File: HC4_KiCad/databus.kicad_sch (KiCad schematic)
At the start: 11 parts, among them IC10 74HC4002, IC8 74HC257, IC9 74HC244, J3 Expantion_Connector

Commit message: 回路の改良　試験は明日やる
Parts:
- added RN2: 10k, Resistor_THT:R_Array_SIP9, symbol Device:R_Network08_Split
- renumbered RN2 to RN1
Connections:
- net Databus0: now also RN2.2 (R1.2)
- net Databus1: now also RN2.3 (R2.2)
- net Databus2: now also RN2.4 (R3.2)
- net Databus3: now also RN2.5 (R4.2)
- net VCC: now also RN2.1 (R1), RN2.1 (R1), RN2.1 (R1), RN2.1 (R1), RN2.1 (R1), RN2.1 (R1), RN2.1 (R1), RN2.1 (R1)
- net Dummy7: now reaches J3.10 (Pin_10)
- net Dummy7: now also RN2.9 (R8.2)
- net Dummy4: now reaches J3.7 (Pin_7)
- net Dummy4: now also RN2.6 (R5.2)
- net Dummy5: now reaches J3.8 (Pin_8)
- net Dummy5: now also RN2.7 (R6.2)
- net Dummy6: now reaches J3.9 (Pin_9)
- net Dummy6: now also RN2.8 (R7.2)
- no-connect marks 22 -> 18

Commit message: フットプリントをSOPに変更
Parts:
- CP8, CP9: footprint Capacitor_THT:C_Disc_D3.0mm_W1.6mm_P2.50mm -> Capacitor_SMD:C_0603_1608Metric
- IC10: footprint Package_DIP:DIP-14_W7.62mm_Socket -> Package_SO:SO-14_5.3x10.2mm_P1.27mm
- IC8: footprint Package_DIP:DIP-16_W7.62mm_Socket -> Package_SO:SO-16_5.3x10.2mm_P1.27mm
- IC9: footprint Package_DIP:DIP-20_W7.62mm_Socket -> Package_SO:SOP-20_7.5x12.8mm_P1.27mm
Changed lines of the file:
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@@
 			)
 		)
-		(property "Footprint" "Capacitor_THT:C_Disc_D3.0mm_W1.6mm_P2.50mm"
+		(property "Footprint" "Capacitor_SMD:C_0603_1608Metric"
 			(at 147.0152 163.83 0)
 			(effects
@@
 			)
 		)
-		(property "Footprint" "Package_DIP:DIP-20_W7.62mm_Socket"
+		(property "Footprint" "Package_SO:SOP-20_7.5x12.8mm_P1.27mm"
 			(at 99.06 133.35 0)
 			(effects
@@
 			)
 		)
-		(property "Footprint" "Package_DIP:DIP-16_W7.62mm_Socket"
+		(property "Footprint" "Package_SO:SO-16_5.3x10.2mm_P1.27mm"
 			(at 99.06 72.39 0)
 			(effects
@@
 			)
 		)
-		(property "Footprint" "Capacitor_THT:C_Disc_D3.0mm_W1.6mm_P2.50mm"
+		(property "Footprint" "Capacitor_SMD:C_0603_1608Metric"
 			(at 153.3652 163.83 0)
 			(effects
@@
 			)
 		)
-		(property "Footprint" "Package_DIP:DIP-14_W7.62mm_Socket"
+		(property "Footprint" "Package_SO:SO-14_5.3x10.2mm_P1.27mm"
 			(at 144.78 64.77 0)
 			(effects

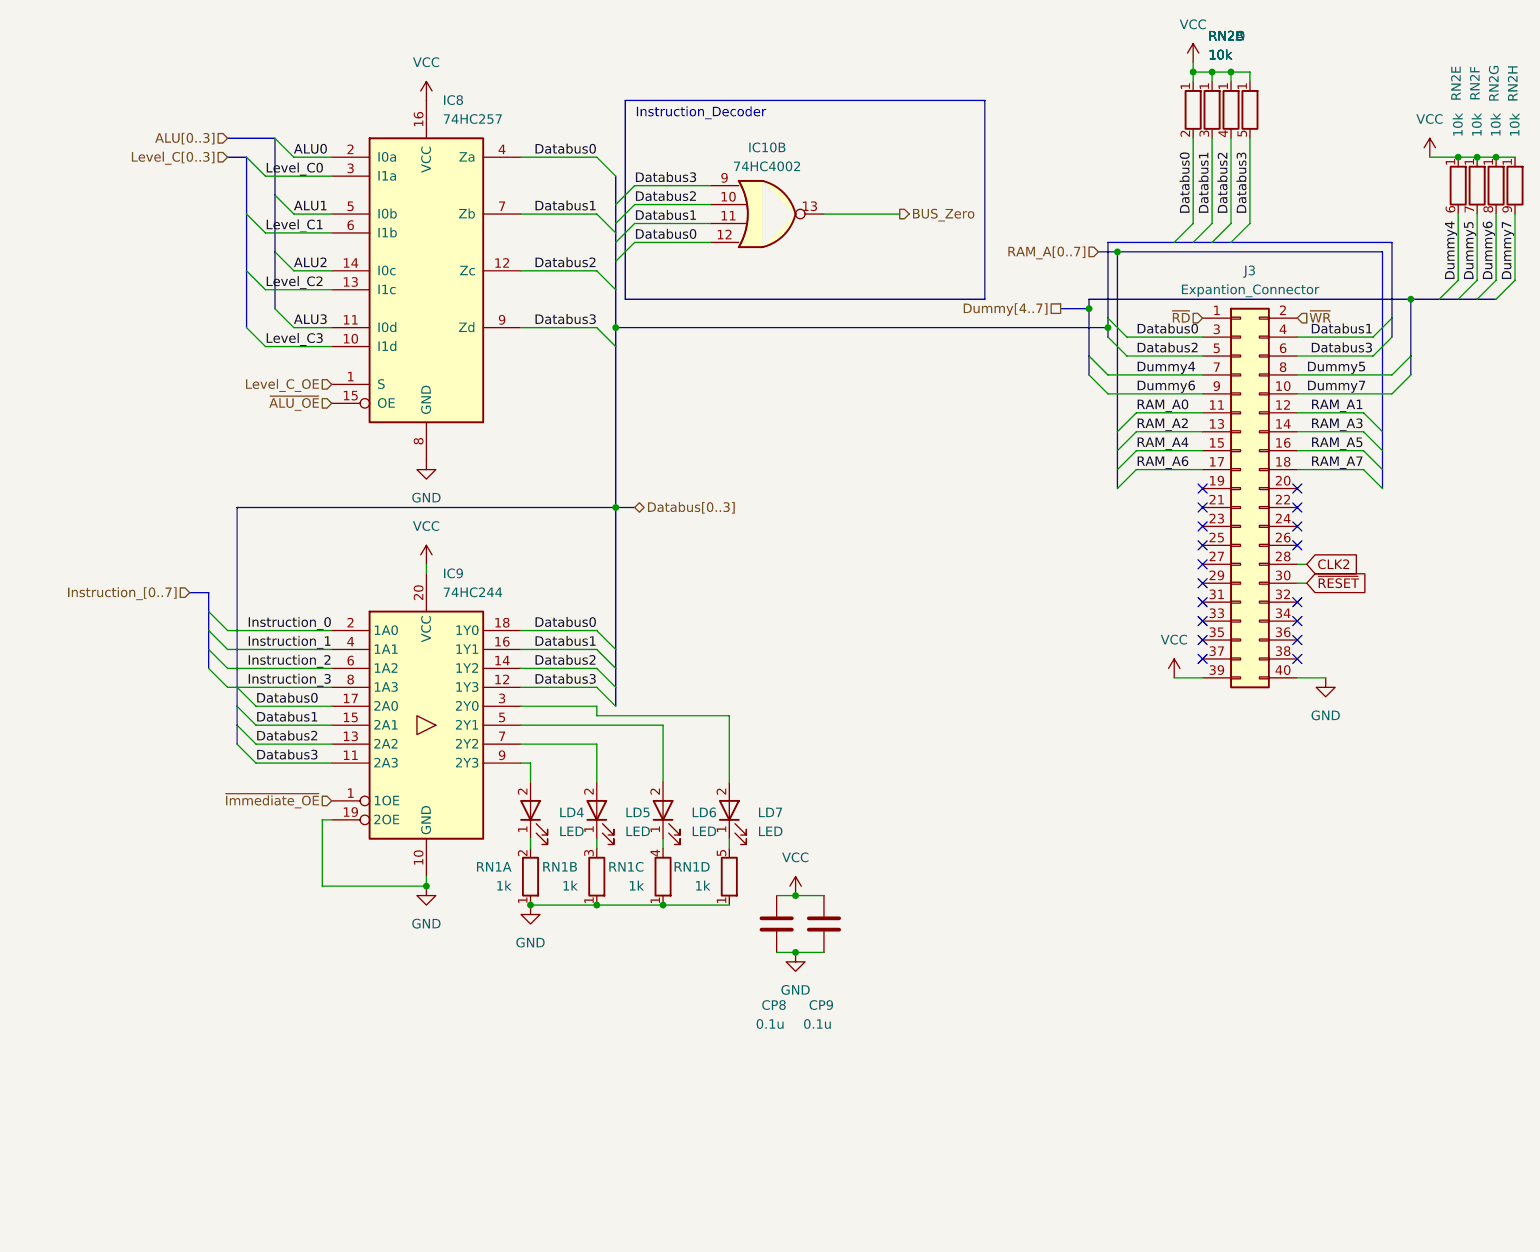
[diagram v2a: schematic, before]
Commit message: Added output port for blink
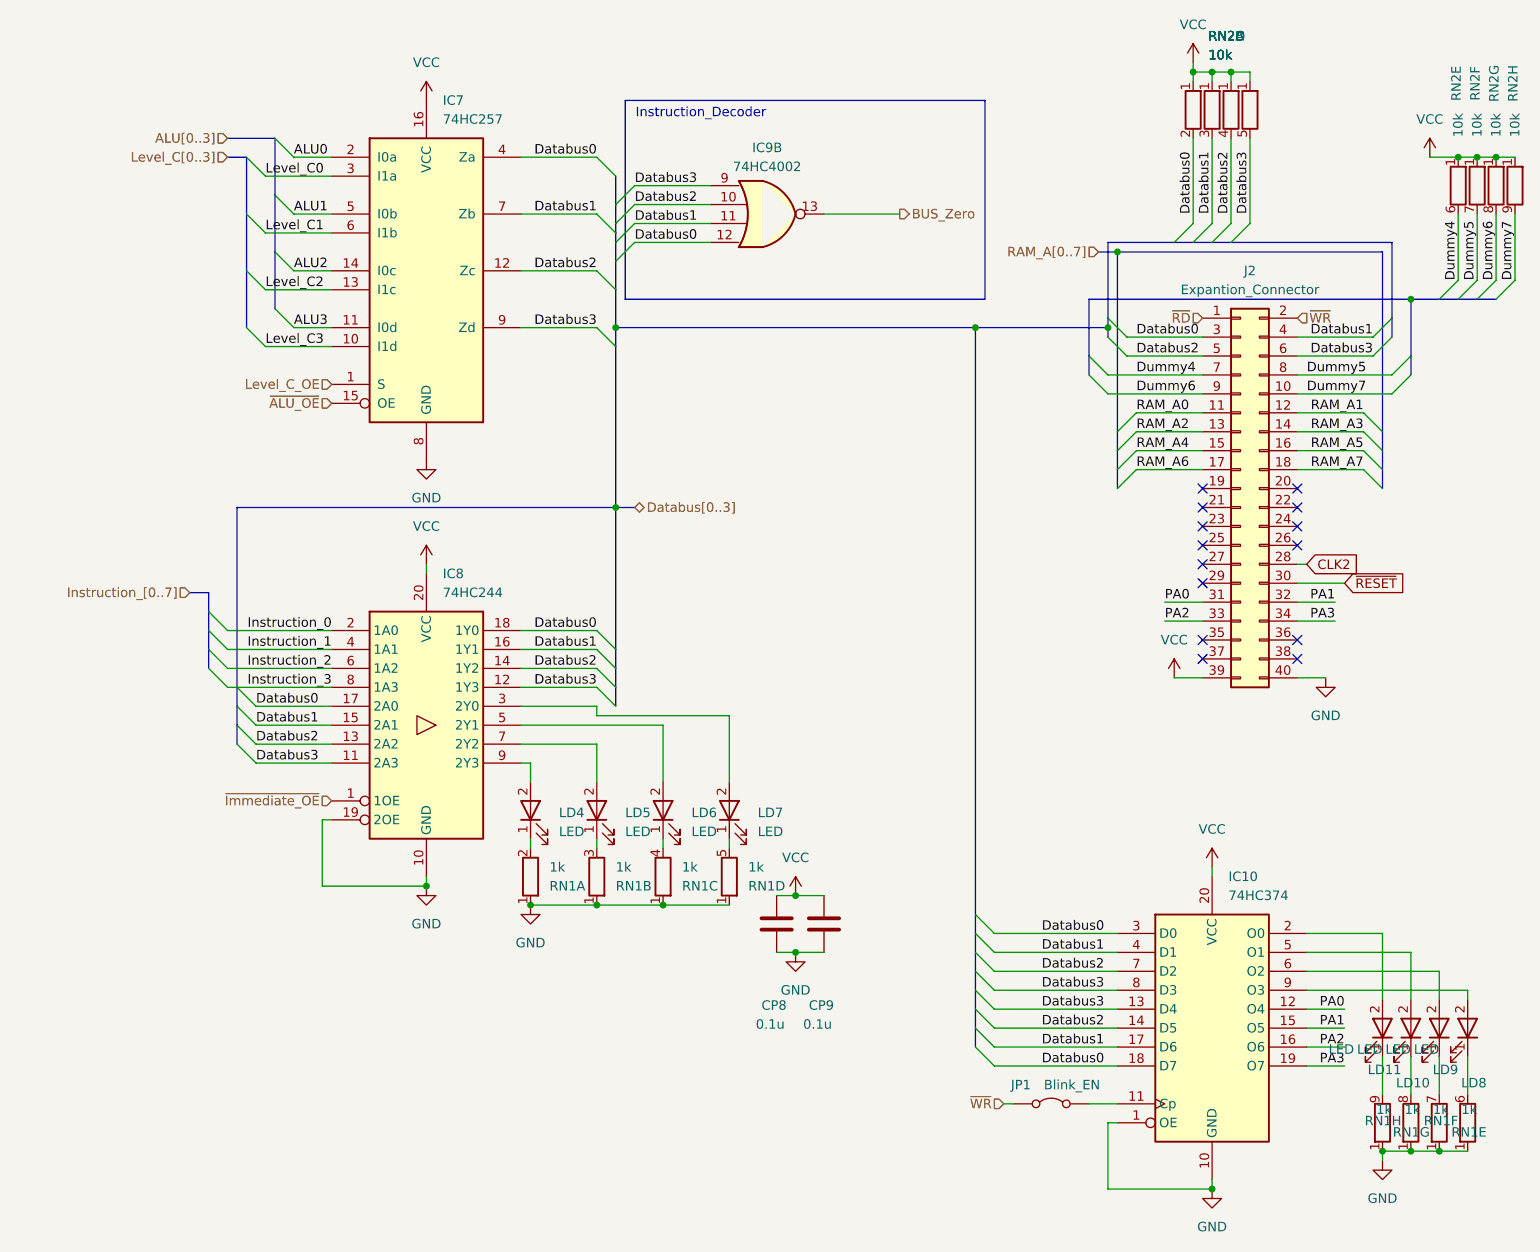
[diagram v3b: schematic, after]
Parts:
- removed RN1: 1k, Resistor_THT:R_Array_SIP5, symbol Device:R_Network04_Split
- added IC10: 74HC374, Package_SO:SOP-20_7.5x12.8mm_P1.27mm, symbol 74xx_2:74HC374
- added JP1: Blink_EN, Connector_PinSocket_2.54mm:PinSocket_1x02_P2.54mm_Vertical, symbol Jumper:Jumper_2_Bridged
- added LD10, LD11, LD8, LD9: LED, LED_THT:LED_Rectangular_W5.0mm_H2.0mm, symbol Device2:LED_
- added RN1: 1k, Resistor_THT:R_Array_SIP9, symbol Device:R_Network08_Split
- renumbered IC8 to IC7, IC9 to IC8, IC10 to IC9, J3 to J2
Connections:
- net Databus0: now also IC10.18 (D7), IC10.3 (D0)
- net Databus1: now also IC10.17 (D6), IC10.4 (D1)
- net Databus2: now also IC10.14 (D5), IC10.7 (D2)
- net Databus3: now also IC10.13 (D4), IC10.8 (D3)
- net GND: now also IC10.1 (OE), IC10.10 (GND), RN1.1 (R1), RN1.1 (R1), RN1.1 (R1), RN1.1 (R1), RN1.1 (R1), RN1.1 (R1), RN1.1 (R1), RN1.1 (R1)
- net VCC: now also IC10.20 (VCC)
- net ~{WR}: now also JP1.1 (A)
- net at LD6.1 (K): now also RN1.4 (R3.2)
- net at LD5.1 (K): now also RN1.3 (R2.2)
- net at LD7.1 (K): now also RN1.5 (R4.2)
- net at LD4.1 (K): now also RN1.2 (R1.2)
- net PA0: now reaches J2.31 (Pin_31)
- net PA0: now also IC10.12 (O4)
- net PA1: now reaches J2.32 (Pin_32)
- net PA1: now also IC10.15 (O5)
- net PA2: now reaches J2.33 (Pin_33)
- net PA2: now also IC10.16 (O6)
- net PA3: now reaches J2.34 (Pin_34)
- net PA3: now also IC10.19 (O7)
- new net: LD9.1 (K), RN1.7 (R6.2)
- new net: IC10.11 (Cp), JP1.2 (B)
- new net: IC10.2 (O0), LD11.2
- new net: IC10.5 (O1), LD10.2
- new net: IC10.6 (O2), LD9.2
- new net: IC10.9 (O3), LD8.2
- new net: LD10.1 (K), RN1.8 (R7.2)
- new net: LD8.1 (K), RN1.6 (R5.2)
- new net: LD11.1 (K), RN1.9 (R8.2)
- no-connect marks 18 -> 14

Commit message: ミスを修正
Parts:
- renumbered LD9 to LD10, LD8 to LD11, LD11 to LD8, LD10 to LD9
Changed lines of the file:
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@@
 		(on_board yes)
 		(dnp no)
-		(property "Reference" "LD10"
+		(property "Reference" "LD9"
 			(at 233.68 181.356 90)
 			(effects
@@
 			(project "HC4_KiCad"
 				(path "/33731ded-38c0-4297-bdd8-92b082f46ff8/294cbb59-ed60-4be2-81ec-3da02c446083"
-					(reference "LD10")
+					(reference "LD9")
 					(unit 1)
 				)
@@
 		(on_board yes)
 		(dnp no)
-		(property "Reference" "LD9"
+		(property "Reference" "LD10"
 			(at 237.49 179.578 90)
 			(effects
@@
 			(project "HC4_KiCad"
 				(path "/33731ded-38c0-4297-bdd8-92b082f46ff8/294cbb59-ed60-4be2-81ec-3da02c446083"
-					(reference "LD9")
+					(reference "LD10")
 					(unit 1)
 				)
@@
 		(on_board yes)
 		(dnp no)
-		(property "Reference" "LD8"
+		(property "Reference" "LD11"
 			(at 241.3 181.356 90)
 			(effects
@@
 			(project ""
 				(path "/33731ded-38c0-4297-bdd8-92b082f46ff8/294cbb59-ed60-4be2-81ec-3da02c446083"
-					(reference "LD8")
+					(reference "LD11")
 					(unit 1)
 				)
@@
 		(on_board yes)
 		(dnp no)
-		(property "Reference" "LD11"
+		(property "Reference" "LD8"
 			(at 229.87 179.578 90)
 			(effects
@@
 			(project "HC4_KiCad"
 				(path "/33731ded-38c0-4297-bdd8-92b082f46ff8/294cbb59-ed60-4be2-81ec-3da02c446083"
-					(reference "LD11")
+					(reference "LD8")
 					(unit 1)
 				)

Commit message: moti
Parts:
- IC6: renamed from IC7; footprint Package_SO:SO-16_5.3x10.2mm_P1.27mm -> Package_DIP:DIP-16_W7.62mm
- IC7: renamed from IC8; footprint Package_SO:SOP-20_7.5x12.8mm_P1.27mm -> Package_DIP:DIP-20_W7.62mm
- IC8: renamed from IC9; footprint Package_SO:SO-14_5.3x10.2mm_P1.27mm -> Package_DIP:DIP-14_W7.62mm
- IC9: renamed from IC10; footprint Package_SO:SOP-20_7.5x12.8mm_P1.27mm -> Package_DIP:DIP-20_W7.62mm
- renumbered CP8 to CP7, CP9 to CP8, J2 to J3
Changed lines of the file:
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@@
 		(dnp no)
 		(fields_autoplaced yes)
-		(property "Reference" "#PWR028"
+		(property "Reference" "#PWR029"
 			(at 199.39 130.81 0)
 			(effects
@@
 			(project ""
 				(path "/33731ded-38c0-4297-bdd8-92b082f46ff8/294cbb59-ed60-4be2-81ec-3da02c446083"
-					(reference "#PWR028")
+					(reference "#PWR029")
 					(unit 1)
 				)
@@
 		(dnp no)
 		(fields_autoplaced yes)
-		(property "Reference" "#PWR021"
+		(property "Reference" "#PWR022"
 			(at 99.06 53.34 0)
 			(effects
@@
 			(project ""
 				(path "/33731ded-38c0-4297-bdd8-92b082f46ff8/294cbb59-ed60-4be2-81ec-3da02c446083"
-					(reference "#PWR021")
+					(reference "#PWR022")
 					(unit 1)
 				)
@@
 		(on_board yes)
 		(dnp no)
-		(property "Reference" "#PWR023"
+		(property "Reference" "#PWR024"
 			(at 99.06 115.57 0)
 			(effects
@@
 			(project ""
 				(path "/33731ded-38c0-4297-bdd8-92b082f46ff8/294cbb59-ed60-4be2-81ec-3da02c446083"
-					(reference "#PWR023")
+					(reference "#PWR024")
 					(unit 1)
 				)
@@
 		(dnp no)
 		(fields_autoplaced yes)
-		(property "Reference" "#PWR024"
+		(property "Reference" "#PWR025"
 			(at 99.06 161.29 0)
 			(effects
@@
 			(project ""
 				(path "/33731ded-38c0-4297-bdd8-92b082f46ff8/294cbb59-ed60-4be2-81ec-3da02c446083"
-					(reference "#PWR024")
+					(reference "#PWR025")
 					(unit 1)
 				)
@@
 		(dnp no)
 		(fields_autoplaced yes)
-		(property "Reference" "#PWR034"
+		(property "Reference" "#PWR035"
 			(at 233.68 60.96 0)
 			(effects
@@
 			(project ""
 				(path "/33731ded-38c0-4297-bdd8-92b082f46ff8/294cbb59-ed60-4be2-81ec-3da02c446083"
-					(reference "#PWR034")
+					(reference "#PWR035")
 					(unit 1)
 				)
@@
 		(dnp no)
 		(fields_autoplaced yes)
-		(property "Reference" "IC10"
+		(property "Reference" "IC9"
 			(at 206.6641 153.67 0)
 			(effects
@@
 			)
 		)
-		(property "Footprint" "Package_SO:SOP-20_7.5x12.8mm_P1.27mm"
+		(property "Footprint" "Package_DIP:DIP-20_W7.62mm"
 			(at 204.47 173.99 0)
 			(effects
@@
 			(project ""
 				(path "/33731ded-38c0-4297-bdd8-92b082f46ff8/294cbb59-ed60-4be2-81ec-3da02c446083"
-					(reference "IC10")
+					(reference "IC9")
 					(unit 1)
 				)
@@
 		(dnp no)
 		(fields_autoplaced yes)
-		(property "Reference" "#PWR022"
+		(property "Reference" "#PWR023"
 			(at 99.06 104.14 0)
 			(effects
@@
 			(project ""
 				(path "/33731ded-38c0-4297-bdd8-92b082f46ff8/294cbb59-ed60-4be2-81ec-3da02c446083"
-					(reference "#PWR022")
+					(reference "#PWR023")
 					(unit 1)
 				)
@@
 		(on_board yes)
 		(dnp no)
-		(property "Reference" "CP8"
+		(property "Reference" "CP7"
 			(at 144.018 170.942 0)
 			(effects
@@
 			(project "HC4_KiCad"
 				(path "/33731ded-38c0-4297-bdd8-92b082f46ff8/294cbb59-ed60-4be2-81ec-3da02c446083"
-					(reference "CP8")
+					(reference "CP7")
 					(unit 1)
 				)
@@
 		(dnp no)
 		(fields_autoplaced yes)
-		(property "Reference" "IC8"
+		(property "Reference" "IC7"
 			(at 101.2541 113.03 0)
 			(effects
@@
 			)
 		)
-		(property "Footprint" "Package_SO:SOP-20_7.5x12.8mm_P1.27mm"
+		(property "Footprint" "Package_DIP:DIP-20_W7.62mm"
 			(at 99.06 133.35 0)
 			(effects
@@
 			(project "HC4_KiCad"
 				(path "/33731ded-38c0-4297-bdd8-92b082f46ff8/294cbb59-ed60-4be2-81ec-3da02c446083"
-					(reference "IC8")
+					(reference "IC7")
 					(unit 1)
 				)
@@
 		(dnp no)
 		(fields_autoplaced yes)
-		(property "Reference" "#PWR029"
+		(property "Reference" "#PWR030"
 			(at 201.93 48.26 0)
 			(effects
@@
 			(project "HC4_KiCad"
 				(path "/33731ded-38c0-4297-bdd8-92b082f46ff8/294cbb59-ed60-4be2-81ec-3da02c446083"
-					(reference "#PWR029")
+					(reference "#PWR030")
 					(unit 1)
 				)
@@
 		(dnp no)
 		(fields_autoplaced yes)
-		(property "Reference" "#PWR031"
+		(property "Reference" "#PWR032"
 			(at 204.47 201.93 0)
 			(effects
@@
 			(project ""
 				(path "/33731ded-38c0-4297-bdd8-92b082f46ff8/294cbb59-ed60-4be2-81ec-3da02c446083"
-					(reference "#PWR031")
+					(reference "#PWR032")
 					(unit 1)
 				)
@@
 		(dnp no)
 		(fields_autoplaced yes)
-		(property "Reference" "IC7"
+		(property "Reference" "IC6"
 			(at 101.2541 49.53 0)
 			(effects
@@
 			)
 		)
-		(property "Footprint" "Package_SO:SO-16_5.3x10.2mm_P1.27mm"
+		(property "Footprint" "Package_DIP:DIP-16_W7.62mm"
 			(at 99.06 72.39 0)
 			(effects
@@
 			(project ""
 				(path "/33731ded-38c0-4297-bdd8-92b082f46ff8/294cbb59-ed60-4be2-81ec-3da02c446083"
-					(reference "IC7")
+					(reference "IC6")
 					(unit 1)
 				)
@@
 		(dnp no)
 		(fields_autoplaced yes)
-		(property "Reference" "#PWR027"
+		(property "Reference" "#PWR028"
 			(at 148.59 170.18 0)
 			(effects
@@
 			(project ""
 				(path "/33731ded-38c0-4297-bdd8-92b082f46ff8/294cbb59-ed60-4be2-81ec-3da02c446083"
-					(reference "#PWR027")
+					(reference "#PWR028")
 					(unit 1)
 				)
@@
 		(dnp no)
 		(fields_autoplaced yes)
-		(property "Reference" "#PWR032"
+		(property "Reference" "#PWR033"
 			(at 219.71 133.35 0)
 			(effects
@@
 			(project ""
 				(path "/33731ded-38c0-4297-bdd8-92b082f46ff8/294cbb59-ed60-4be2-81ec-3da02c446083"
-					(reference "#PWR032")
+					(reference "#PWR033")
 					(unit 1)
 				)
@@
 		(dnp no)
 		(fields_autoplaced yes)
-		(property "Reference" "#PWR033"
+		(property "Reference" "#PWR034"
 			(at 227.33 198.12 0)
 			(effects
@@
 			(project ""
 				(path "/33731ded-38c0-4297-bdd8-92b082f46ff8/294cbb59-ed60-4be2-81ec-3da02c446083"
-					(reference "#PWR033")
+					(reference "#PWR034")
 					(unit 1)
 				)
@@
 		(dnp no)
 		(fields_autoplaced yes)
-		(property "Reference" "#PWR025"
+		(property "Reference" "#PWR026"
 			(at 113.03 163.83 0)
 			(effects
@@
 			(project "HC4_KiCad"
 				(path "/33731ded-38c0-4297-bdd8-92b082f46ff8/294cbb59-ed60-4be2-81ec-3da02c446083"
-					(reference "#PWR025")
+					(reference "#PWR026")
 					(unit 1)
 				)
@@
 		(dnp no)
 		(fields_autoplaced yes)
-		(property "Reference" "#PWR026"
+		(property "Reference" "#PWR027"
 			(at 148.59 160.02 0)
 			(effects
@@
 			(project ""
 				(path "/33731ded-38c0-4297-bdd8-92b082f46ff8/294cbb59-ed60-4be2-81ec-3da02c446083"
-					(reference "#PWR026")
+					(reference "#PWR027")
 					(unit 1)
 				)
@@
 		(on_board yes)
 		(dnp no)
-		(property "Reference" "CP9"
+		(property "Reference" "CP8"
 			(at 150.368 170.942 0)
 			(effects
@@
 			(project "HC4_KiCad"
 				(path "/33731ded-38c0-4297-bdd8-92b082f46ff8/294cbb59-ed60-4be2-81ec-3da02c446083"
-					(reference "CP9")
+					(reference "CP8")
 					(unit 1)
 				)
@@
 		(dnp no)
 		(fields_autoplaced yes)
-		(property "Reference" "IC9"
+		(property "Reference" "IC8"
 			(at 144.78 55.88 0)
 			(effects
@@
 			)
 		)
-		(property "Footprint" "Package_SO:SO-14_5.3x10.2mm_P1.27mm"
+		(property "Footprint" "Package_DIP:DIP-14_W7.62mm"
 			(at 144.78 64.77 0)
 			(effects
@@
 			(project "HC4_KiCad"
 				(path "/33731ded-38c0-4297-bdd8-92b082f46ff8/294cbb59-ed60-4be2-81ec-3da02c446083"
-					(reference "IC9")
+					(reference "IC8")
 					(unit 2)
 				)
@@
 		(dnp no)
 		(fields_autoplaced yes)
-		(property "Reference" "#PWR030"
+		(property "Reference" "#PWR031"
 			(at 204.47 156.21 0)
 			(effects
@@
 			(project ""
 				(path "/33731ded-38c0-4297-bdd8-92b082f46ff8/294cbb59-ed60-4be2-81ec-3da02c446083"
-					(reference "#PWR030")
+					(reference "#PWR031")
 					(unit 1)
 				)
@@
 		(dnp no)
 		(fields_autoplaced yes)
-		(property "Reference" "J2"
+		(property "Reference" "J3"
 			(at 209.55 72.39 0)
 			(effects
@@
 			(project "HC4_KiCad"
 				(path "/33731ded-38c0-4297-bdd8-92b082f46ff8/294cbb59-ed60-4be2-81ec-3da02c446083"
-					(reference "J2")
+					(reference "J3")
 					(unit 1)
 				)
